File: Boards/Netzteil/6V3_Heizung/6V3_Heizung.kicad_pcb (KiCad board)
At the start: 2 copper layers, 100 x 80 mm, 37 parts, among them P1 7V5_AC, P2 12V_DC, P3 6V3_DC_1, P4 6V3_DC_2, Q1 IRF540N, Q2 IRF540N, U1 TL072

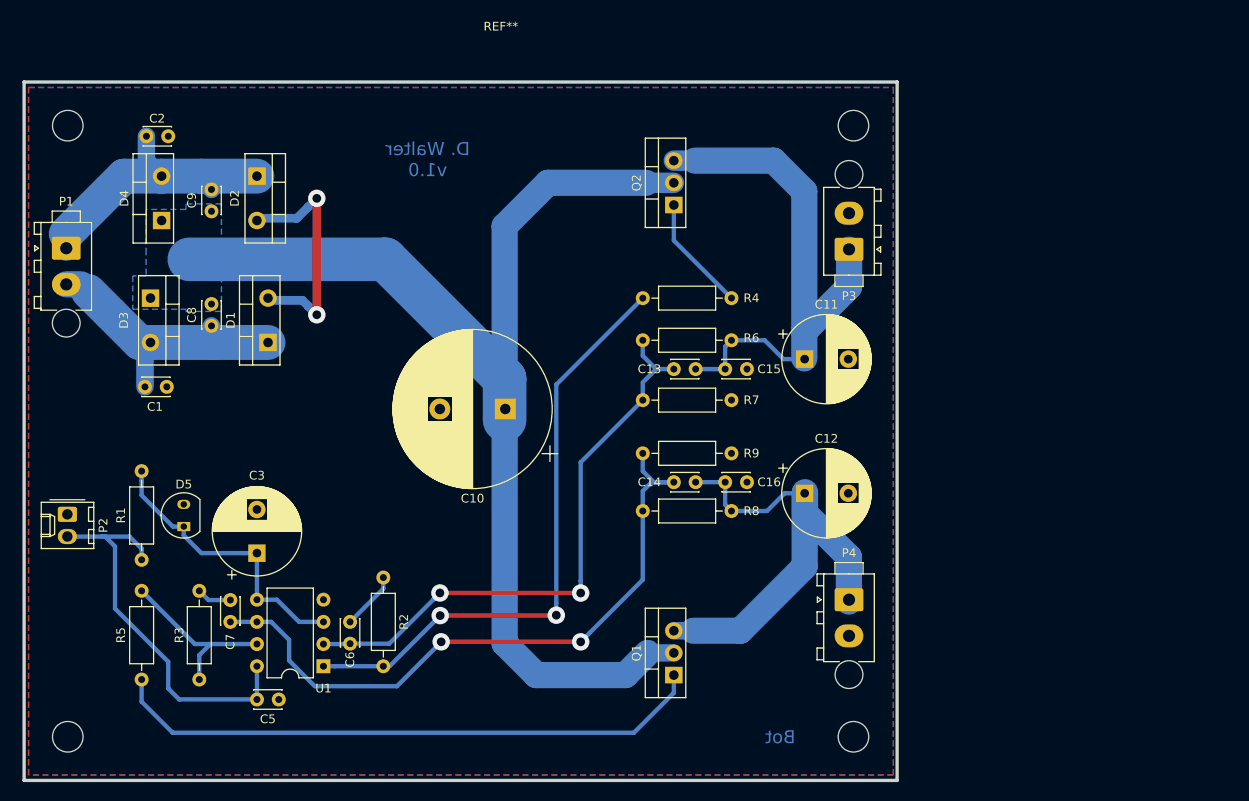
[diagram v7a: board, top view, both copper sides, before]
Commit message: HV Switch on delay added
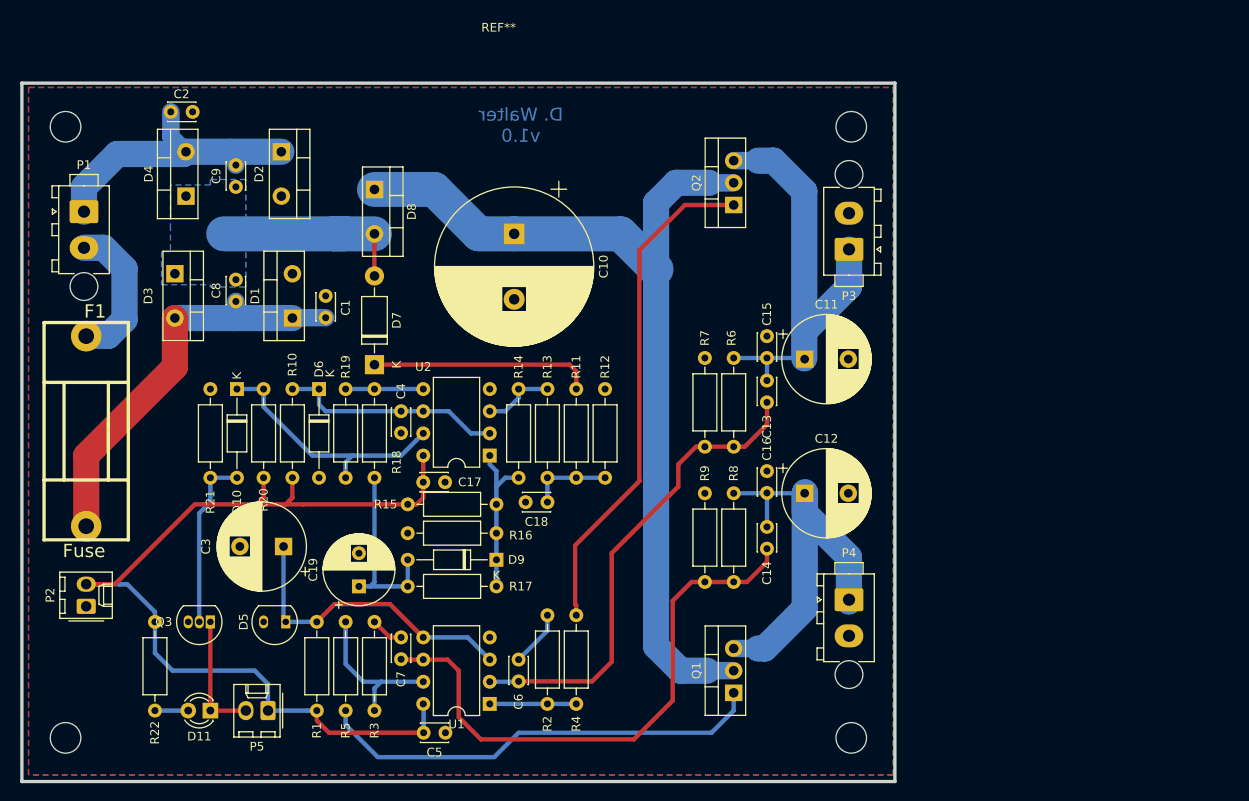
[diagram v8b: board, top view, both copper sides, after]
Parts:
- added C17: 100nF / 63V, Capacitor_THT:C_Disc_D3.0mm_W2.0mm_P2.50mm, F.Cu at (105.5, 84.6)
- added C18: 1µF / 16V, Capacitor_THT:C_Disc_D3.0mm_W2.0mm_P2.50mm, F.Cu at (119.8, 86.9)
- added C19: 47µF / 16V, Capacitor_THT:CP_Radial_D8.0mm_P3.80mm, F.Cu at (98.2, 96.5)
- added C4: 100nF / 63V, Capacitor_THT:C_Disc_D3.0mm_W2.0mm_P2.50mm, F.Cu at (103.0, 76.5)
- added D10: ZD5V6, Diode_THT:D_DO-35_SOD27_P10.16mm_Horizontal, F.Cu at (84.2, 73.9)
- added D11: LED, LED_THT:LED_D3.0mm, F.Cu at (81.2, 110.7)
- added D6: ZD3V9, Diode_THT:D_DO-35_SOD27_P10.16mm_Horizontal, F.Cu at (93.6, 73.9)
- added D7: SB190, Diode_THT:D_DO-41_SOD81_P10.16mm_Horizontal, F.Cu at (99.9, 71.1)
- added D8: 18TQ045, Package_TO_SOT_THT:TO-220-2_Vertical, F.Cu at (99.9, 51.1)
- added D9: 1N4148, Diode_THT:D_DO-35_SOD27_P10.16mm_Horizontal, F.Cu at (113.9, 93.5)
- added F1: Fuse, w_misc_comp:fuse_holder_CQ-2, F.Cu at (66.9, 78.7)
- added P5: Relais, Connector_Molex:Molex_KK-254_AE-6410-02A_1x02_P2.54mm_Vertical, F.Cu at (87.8, 110.7)
- added Q3: BS170, Package_TO_SOT_THT:TO-92_Inline, F.Cu at (81.2, 100.6)
- added R10: 4K7, Resistor_THT:R_Axial_DIN0207_L6.3mm_D2.5mm_P10.16mm_Horizontal, F.Cu at (90.6, 84.1)
- added R11: 82K, Resistor_THT:R_Axial_DIN0207_L6.3mm_D2.5mm_P10.16mm_Horizontal, F.Cu at (123.1, 73.9)
- added R12: 100K, Resistor_THT:R_Axial_DIN0207_L6.3mm_D2.5mm_P10.16mm_Horizontal, F.Cu at (126.4, 84.1)
- added R13: 10K, Resistor_THT:R_Axial_DIN0207_L6.3mm_D2.5mm_P10.16mm_Horizontal, F.Cu at (119.8, 73.9)
- added R14: 1M, Resistor_THT:R_Axial_DIN0207_L6.3mm_D2.5mm_P10.16mm_Horizontal, F.Cu at (116.5, 84.1)
- added R15: 10K, Resistor_THT:R_Axial_DIN0207_L6.3mm_D2.5mm_P10.16mm_Horizontal, F.Cu at (113.9, 87.1)
- added R16: 10K, Resistor_THT:R_Axial_DIN0207_L6.3mm_D2.5mm_P10.16mm_Horizontal, F.Cu at (103.8, 90.4)
- added R17: 470K, Resistor_THT:R_Axial_DIN0207_L6.3mm_D2.5mm_P10.16mm_Horizontal, F.Cu at (113.9, 96.5)
- added R18: 10K, Resistor_THT:R_Axial_DIN0207_L6.3mm_D2.5mm_P10.16mm_Horizontal, F.Cu at (99.9, 84.1)
- added R19: 5M1, Resistor_THT:R_Axial_DIN0207_L6.3mm_D2.5mm_P10.16mm_Horizontal, F.Cu at (96.6, 73.9)
- added R20: 10K, Resistor_THT:R_Axial_DIN0207_L6.3mm_D2.5mm_P10.16mm_Horizontal, F.Cu at (87.2, 84.1)
- added R21: 10K, Resistor_THT:R_Axial_DIN0207_L6.3mm_D2.5mm_P10.16mm_Horizontal, F.Cu at (81.2, 84.1)
- added R22: 47k, Resistor_THT:R_Axial_DIN0207_L6.3mm_D2.5mm_P10.16mm_Horizontal, F.Cu at (74.8, 100.6)
- added U2: LM393, Package_DIP:DIP-8_W7.62mm, F.Cu at (113.2, 81.5)
- moved R4 40.4 mm to (123.1, 99.8), turned to 270 degrees
- moved R1 26.5 mm to (93.3, 110.7)
- moved R5 23.6 mm to (96.6, 110.7)
- moved C1 22.2 mm to (94.4, 65.7), turned to 90 degrees
- moved R3 20.4 mm to (99.9, 100.6)
- moved C10 20.1 mm to (116.0, 56.1), turned to 270 degrees
- moved C7 20.0 mm to (103.0, 102.4)
- moved C6 19.8 mm to (116.5, 104.9)
- moved U1 19.5 mm to (113.2, 110.0)
- moved C5 19.5 mm to (108.1, 113.3)
- moved R2 19.3 mm to (119.8, 99.8)
- moved R6 16.0 mm to (141.1, 80.5), turned to 90 degrees
- moved D5 16.0 mm to (89.8, 100.6), turned to 180 degrees
- moved R8 13.2 mm to (141.1, 96.0), turned to 90 degrees
- moved C14 13.1 mm to (144.9, 92.2), turned to 90 degrees
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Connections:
- C8 pad 2: /V_Unreg -> Net-(C8-Pad2)
- C9 pad 1: /V_Unreg -> Net-(C8-Pad2)
- D3 pad 1: /V_Unreg -> Net-(C8-Pad2)
- D4 pad 1: /V_Unreg -> Net-(C8-Pad2)
- P1 pad 2: Net-(C1-Pad1) -> Net-(F1-Pad2)
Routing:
- net +12V: track 45.4 -> 111.1 mm
- net Net-(R2-Pad2): track 69.9 -> 9.91 mm, vias 2 -> 0
- net Net-(Q2-Pad1): track 13.4 -> 57.8 mm
- net Net-(D10-Pad1): track 0.00 -> 29.6 mm
- net /V_Unreg: track 137.7 -> 108.9 mm
- net GND: track 27.7 -> 0.00 mm, vias 2 -> 0
- net /Vref: track 0.00 -> 25.8 mm
- net Net-(D7-Pad1): track 0.00 -> 25.5 mm
- net Net-(C8-Pad2): track 0.00 -> 23.5 mm
- net Net-(C19-Pad1): track 0.00 -> 21.3 mm
- net Net-(D10-Pad2): track 0.00 -> 20.1 mm
- net Net-(D9-Pad1): track 0.00 -> 18.3 mm
- net Net-(Q1-Pad1): track 68.9 -> 51.9 mm
- net Net-(F1-Pad2): track 0.00 -> 16.7 mm
- net Net-(C1-Pad1): track 31.1 -> 47.4 mm
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- added copper zone on B.Cu, net Net-(C8-Pad2)
- removed copper zone on B.Cu, net /V_Unreg
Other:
- board text removed: "Bot"
